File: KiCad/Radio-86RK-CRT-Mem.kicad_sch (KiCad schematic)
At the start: 20 parts, among them J1 Video, Q1 2N3904, U10 2716/КР573РФ5, U11 2716/КР573РФ5, U13 74198/К155ИР13, U15 7492/К155ИЕ4, U16 7486/К155ЛП5, U17 7474/К155ТМ2, U18 7408/К155ЛИ1, U19 7404/К155ЛН1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

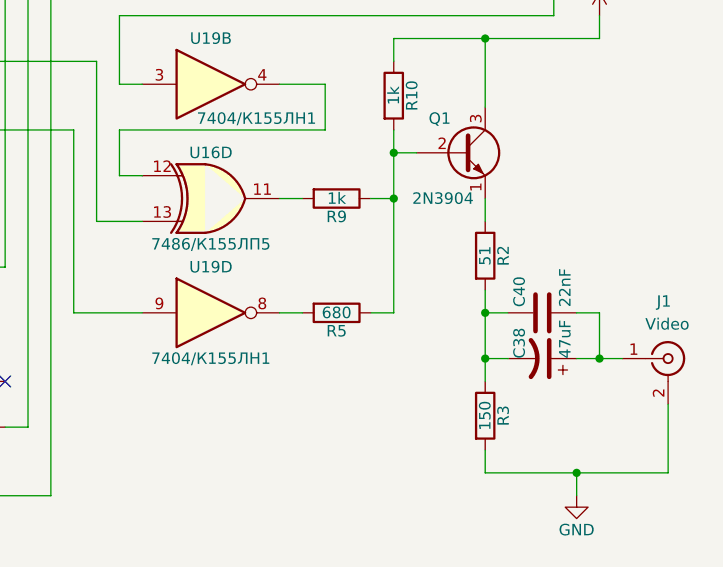
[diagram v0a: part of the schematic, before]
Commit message: Updates for version v1.3: Update silkscreen and resistors values in video generation circuit
Signed-off-by: Sergey Kiselev <skiselev@gmail.com>
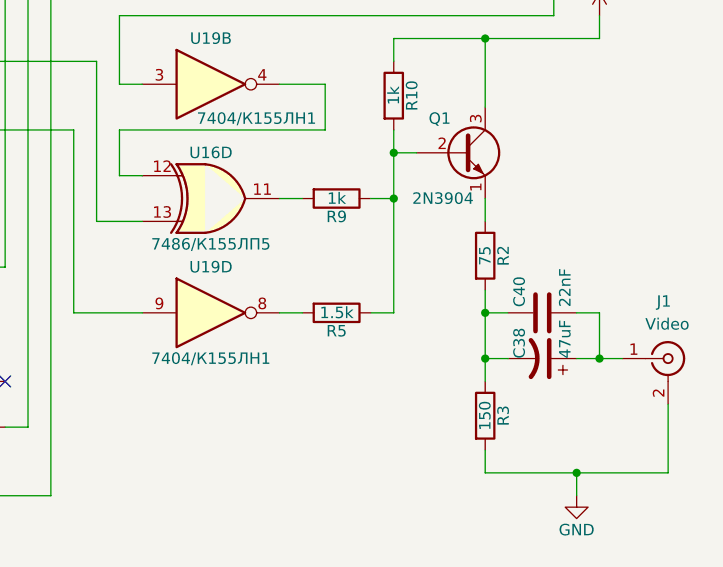
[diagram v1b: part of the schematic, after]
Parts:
- R2: value 51 -> 75
- R5: value 680 -> 1.5k
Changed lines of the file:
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@@
   (title_block
     (title "Radio-86RK")
-    (date "2022-05-11")
-    (rev "1.2")
+    (date "2022-05-13")
+    (rev "1.3")
     (company "Designed by Sergey Kiselev")
     (comment 1 "Based on the previous work by Alexey Khudyakov and Radio magazine publications")
@@
     (in_bom yes) (on_board yes)
     (property "Reference" "R5" (id 0) (at 227.33 146.812 90))
-    (property "Value" "680" (id 1) (at 227.33 144.78 90))
+    (property "Value" "1.5k" (id 1) (at 227.33 144.78 90))
     (property "Footprint" "My_Components:Res_762" (id 2) (at 227.33 143.002 90)
       (effects (font (size 1.27 1.27)) hide)
@@
     (in_bom yes) (on_board yes)
     (property "Reference" "R2" (id 0) (at 245.872 138.43 90))
-    (property "Value" "51" (id 1) (at 243.84 138.43 90))
+    (property "Value" "75" (id 1) (at 243.84 138.43 90))
     (property "Footprint" "My_Components:Res_762" (id 2) (at 242.062 138.43 90)
       (effects (font (size 1.27 1.27)) hide)

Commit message: Add Version 1.4 files
Signed-off-by: Sergey Kiselev <skiselev@gmail.com>
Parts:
- removed U11: 2716/КР573РФ5, My_Components:IC_DIP24_600, symbol my_components:2716
- added JP1: U10 EPROM Type, My_Components:Conn_Pin_Header_4x1_2.54mm, symbol Connector_Generic:Conn_01x04
- added JP2: U11 EPROM Type, My_Components:Conn_Pin_Header_4x1_2.54mm, symbol Connector_Generic:Conn_01x04
- added U11: 2764/К573РФ6/28C64, My_Components:IC_DIP28_600, symbol my_components:27C64
- U10: value 2716/КР573РФ5 -> 2764/К573РФ6/28C64; footprint My_Components:IC_DIP24_600 -> My_Components:IC_DIP28_600; symbol my_components:2716 -> my_components:27C64
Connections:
- net A0: now also U10.10 (A0); no longer U10.8 (A0)
- net A1: now also U10.9 (A1); no longer U10.7 (A1)
- net A10: now also U10.21 (A10); no longer U10.19 (A10)
- net A11: now also JP1.4 (Pin_4)
- net A12: now also U10.2 (A12)
- net A2: now also U10.8 (A2); no longer U10.6 (A2)
- net A3: now also U10.7 (A3); no longer U10.5 (A3)
- net A4: now also U10.6 (A4); no longer U10.4 (A4)
- net A5: now also U10.5 (A5); no longer U10.3 (A5)
- net A6: now also U10.4 (A6); no longer U10.2 (A6)
- net A7: now also U10.3 (A7); no longer U10.1 (A7)
- net A8: now also U10.25 (A8); no longer U10.23 (A8)
- net A9: now also U10.24 (A9); no longer U10.22 (A9)
- net D0: now also U10.11 (DQ0); no longer U10.9 (DQ0)
- net D1: now also U10.12 (DQ1); no longer U10.10 (DQ1)
- net D2: now also U10.13 (DQ2); no longer U10.11 (DQ2)
- net D3: now also U10.15 (DQ3); no longer U10.13 (DQ3)
- net D4: now also U10.16 (DQ4); no longer U10.14 (DQ4)
- net D5: now also U10.17 (DQ5); no longer U10.15 (DQ5)
- net D6: now also U10.18 (DQ6); no longer U10.16 (DQ6)
- net D7: now also U10.19 (DQ7); no longer U10.17 (DQ7)
- net GND: now also U10.14 (GND), U11.14 (GND), U11.2 (A12), U11.22 (~{OE}); no longer U10.12 (GND)
- net VCC: now also U10.26 (NC), U10.27 (~{PGM}), U10.28 (VCC), JP1.2 (Pin_2), JP2.2 (Pin_2), U11.26 (NC), U11.27 (~{PGM}), U11.28 (VCC); no longer U10.21 (VPP), U10.24 (VCC)
- net ~{RD}: now also U10.22 (~{OE}); no longer U10.20 (~{OE})
- net ~{ROM_CS}: now also U10.20 (~{CE}); no longer U10.18 (~{CE})
- net at U8.27 (CC4): now also U11.3 (A7)
- net at RN1.7 (R6), U13.5 (B): now also U11.12 (DQ1)
- net at RN1.9 (R8), U13.7 (C): now also U11.13 (DQ2)
- net at RN1.10 (R9), U13.9 (D): now also U11.15 (DQ3)
- net at RN1.8 (R7), U13.15 (E): now also U11.16 (DQ4)
- net at RN1.6 (R5), U13.17 (F): now also U11.17 (DQ5)
- net at U8.35 (VSP): now also U11.20 (~{CE})
- net at U8.33 (GPA0): now also U11.21 (A10)
- net at U8.26 (CC3): now also U11.4 (A6)
- net at U8.29 (CC6): now also U11.24 (A9)
- net at U8.28 (CC5): now also U11.25 (A8)
- net at U8.25 (CC2): now also U11.5 (A5)
- net at U8.24 (CC1): now also U11.6 (A4)
- net at U8.23 (CC0): now also U11.7 (A3)
- net at U8.2 (LC2): now also U11.8 (A2)
- net at U8.3 (LC1): now also U11.9 (A1)
- net at U8.4 (LC0): now also U11.10 (A0)
- net at RN1.5 (R4), U13.3 (A): now also U11.11 (DQ0)
- net at U8.34 (GPA1): now also JP2.4 (Pin_4)
- new net: JP1.1 (Pin_1), U10.1 (VPP)
- new net: JP2.1 (Pin_1), U11.1 (VPP)
- new net: JP2.3 (Pin_3), U11.23 (A11)
- new net ROM_A11: JP1.3 (Pin_3), U10.23 (A11)
- no-connect marks 17 -> 16
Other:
- note added: "2716 К573РФ2 К573РФ5 2732"
- note added: "EPROM Type Selection JP1 - U10, JP2 - U11: 2-3: 2716, К573РФ2, К573РФ5 1-2,3-4: 2732, 2764, К573РФ6 3-4: 28C64"
- moved on the sheet: R5, R9, RN1, U13, U15, U16B, U16D, U17A, U18C, U19B, U19D
